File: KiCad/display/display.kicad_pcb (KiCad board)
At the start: 2 copper layers, 19 parts, among them J1 Barrel_Jack_Switch, J10 Conn_01x02_Pin, J2 Conn_01x03_Pin, J3 Conn_01x04_Pin, J4 Conn_01x05_Pin, J5 Conn_01x06_Pin, J6 Conn_01x07_Pin, J7 Conn_01x08_Pin, J8 Conn_01x09_Pin, J9 Conn_01x10_Pin, SW1 Cherry Switch Single, SW2 Cherry Switch 1.5x - Enter Key, U2 TMC2209, U3 Display, U4 ICM-20948, U5 24LC512, U6 Adafruit_ICM20948, U7 LTV-817S

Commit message: PCB designs started
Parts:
- removed J10: Conn_01x02_Pin, Connector_JST:JST_PH_B2B-PH-K_1x02_P2.00mm_Vertical
- removed J2: Conn_01x03_Pin, Connector_JST:JST_PH_B3B-PH-K_1x03_P2.00mm_Vertical
- removed J3: Conn_01x04_Pin, Connector_JST:JST_PH_B4B-PH-K_1x04_P2.00mm_Vertical
- removed J4: Conn_01x05_Pin, Connector_JST:JST_PH_B5B-PH-K_1x05_P2.00mm_Vertical
- removed J5: Conn_01x06_Pin, Connector_JST:JST_PH_B6B-PH-K_1x06_P2.00mm_Vertical
- removed J6: Conn_01x07_Pin, Connector_JST:JST_PH_B7B-PH-K_1x07_P2.00mm_Vertical
- removed J7: Conn_01x08_Pin, Connector_JST:JST_PH_B8B-PH-K_1x08_P2.00mm_Vertical
- removed J8: Conn_01x09_Pin, Connector_JST:JST_PH_B9B-PH-K_1x09_P2.00mm_Vertical
- removed J9: Conn_01x10_Pin, Connector_JST:JST_PH_B10B-PH-K_1x10_P2.00mm_Vertical
- removed SW1: Cherry Switch Single, ComponentLib:SW_Cherry_MX_1.00u_PCB
- removed SW2: Cherry Switch 1.5x - Enter Key, ComponentLib:SW_Cherry_MX_1.50u_PCB
- removed U2: TMC2209, ComponentLib:TMC2209 Silentstepstick
- removed U3: Display, ComponentLib:NHD-2.23-12832UCB3
- removed U4: ICM-20948, ComponentLib:ICM-20948
- removed U5: 24LC512, Package_SO:SOIC-8_5.3x6.2mm_P1.27mm
- removed U6: Adafruit_ICM20948, ComponentLib:Adafruit-ICM-20948
- removed U7: LTV-817S, Package_DIP:SMDIP-4_W9.53mm
- added D1: LED, Diode_SMD:D_0603_1608Metric, F.Cu at (126.8, 109.0)
- added JP1: SolderJumper_2_Open, Resistor_SMD:R_0603_1608Metric_Pad0.98x0.95mm_HandSolder, F.Cu at (143.5, 115.2)
- added R1: 15k, Resistor_SMD:R_0603_1608Metric_Pad0.98x0.95mm_HandSolder, F.Cu at (143.5, 119.0)
- added R2: 150R, Resistor_SMD:R_0603_1608Metric, F.Cu at (126.8, 113.5)
- added R3: 2k2, Resistor_SMD:R_0603_1608Metric, F.Cu at (134.0, 115.2)
- added R4: 2k2, Resistor_SMD:R_0603_1608Metric, F.Cu at (139.5, 115.2)
- J1: value Barrel_Jack_Switch -> Conn_01x05_Pin; footprint Connector_BarrelJack:BarrelJack_Wuerth_694106106102_2.0x5.5mm -> Connector_JST:JST_PH_B5B-PH-K_1x05_P2.00mm_Vertical
- U1: value ~ -> Display; footprint ComponentLib:NUCLEO-F767ZI -> ComponentLib:NHD-2.23-12832UCB3; moved to B.Cu
- moved U1 217.2 mm to (130.5, 104.5), turned to 180 degrees
- moved J1 50.8 mm to (122.5, 109.5), turned to 180 degrees
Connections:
- J1 pad 1: unconnected-(J1-Pad1) -> /SCL
- J1 pad 2: unconnected-(J1-Pad2) -> /SDA
- J1 pad 3: unconnected-(J1-Pad3) -> +3V3
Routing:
- net +3V3: track 0.00 -> 70.6 mm
- net /SCL: track 0.00 -> 32.2 mm
- net /SDA: track 0.00 -> 29.8 mm
- net /~{RES}: track 0.00 -> 14.9 mm
- net /A0: track 0.00 -> 8.92 mm
- net Net-(D1-A): track 0.00 -> 2.94 mm
- net GND: vias 0 -> 74
- added copper zone on B.Cu, net /SDA
- added copper zone on B.Cu, net GND
- added copper zone on F.Cu, net GND
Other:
- board outline added: 64 x 44 mm
- board text added: "3V3"
- board text added: "A0 low (JP1 open) : addr = 0b0111100 A0 high (JP1 closed): addr = 0b0111101 R3, R4: Optional I2C pull-up"
- board text added: "GND"
- board text added: "SCL"
- board text added: "SDA"
- board text added: "~{RES}"

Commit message: documentation
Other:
- board size 64 x 44 mm -> 66.2 x 47.1 mm

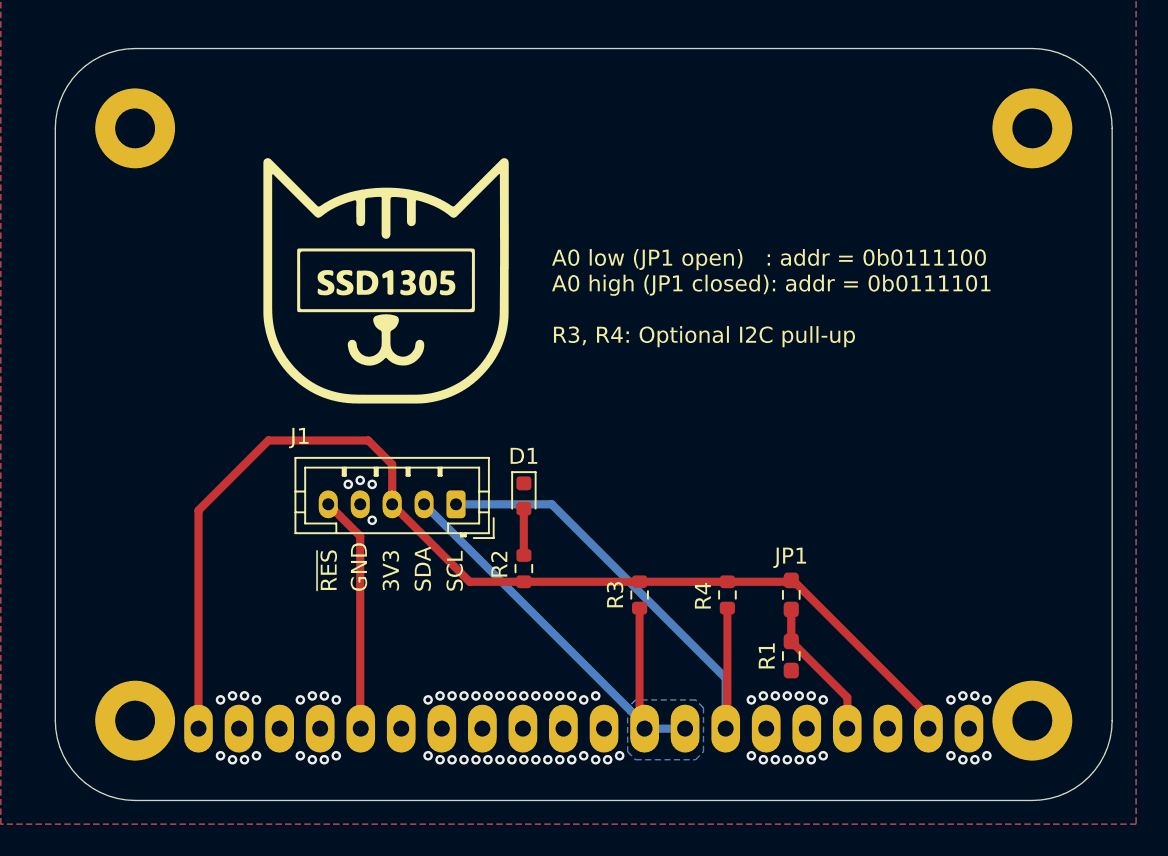
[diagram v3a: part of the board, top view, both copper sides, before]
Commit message: PCB bugfixes based on review
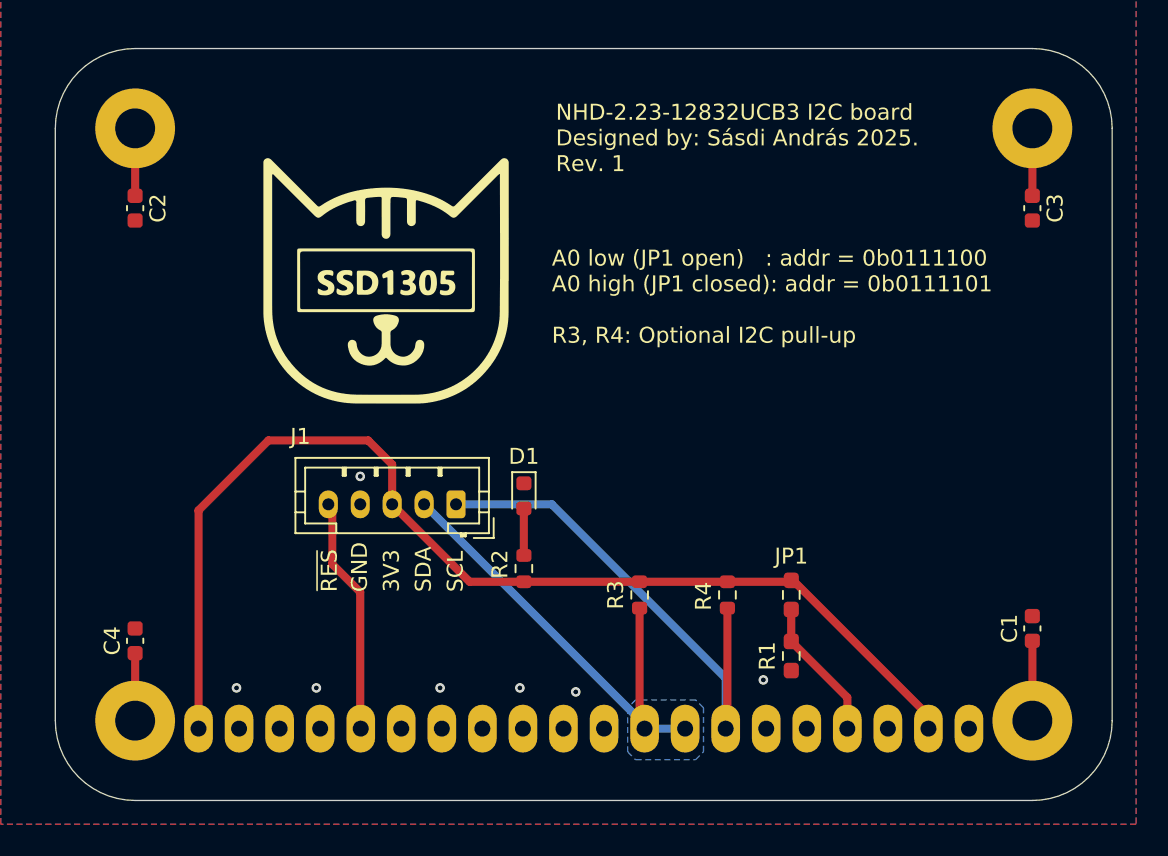
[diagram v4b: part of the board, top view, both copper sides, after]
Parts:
- added C1: 1n, Capacitor_SMD:C_0603_1608Metric, F.Cu at (158.6, 117.3)
- added C2: 1n, Capacitor_SMD:C_0603_1608Metric, F.Cu at (102.4, 91.0)
- added C3: 1n, Capacitor_SMD:C_0603_1608Metric, F.Cu at (158.6, 91.0)
- added C4: 1n, Capacitor_SMD:C_0603_1608Metric, F.Cu at (102.4, 118.0)
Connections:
- U1 pad CH1: unconnected-(U1-PadCH1) -> Net-(C3-Pad1)
- U1 pad CH2: unconnected-(U1-PadCH2) -> Net-(C2-Pad1)
- U1 pad CH3: unconnected-(U1-PadCH3) -> Net-(C1-Pad1)
- U1 pad CH4: unconnected-(U1-PadCH4) -> Net-(C4-Pad1)
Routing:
- net Net-(C1-Pad1): track 0.00 -> 5.00 mm
- net Net-(C4-Pad1): track 0.00 -> 4.22 mm
- net Net-(C3-Pad1): track 0.00 -> 4.22 mm
- net Net-(C2-Pad1): track 0.00 -> 4.22 mm
- net GND: vias 74 -> 7
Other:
- board text added: "NHD-2.23-12832UCB3 I2C board Designed by: Sásdi András 2025. Rev. 1"
